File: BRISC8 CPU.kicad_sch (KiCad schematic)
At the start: 1 part, among them U101 27C256

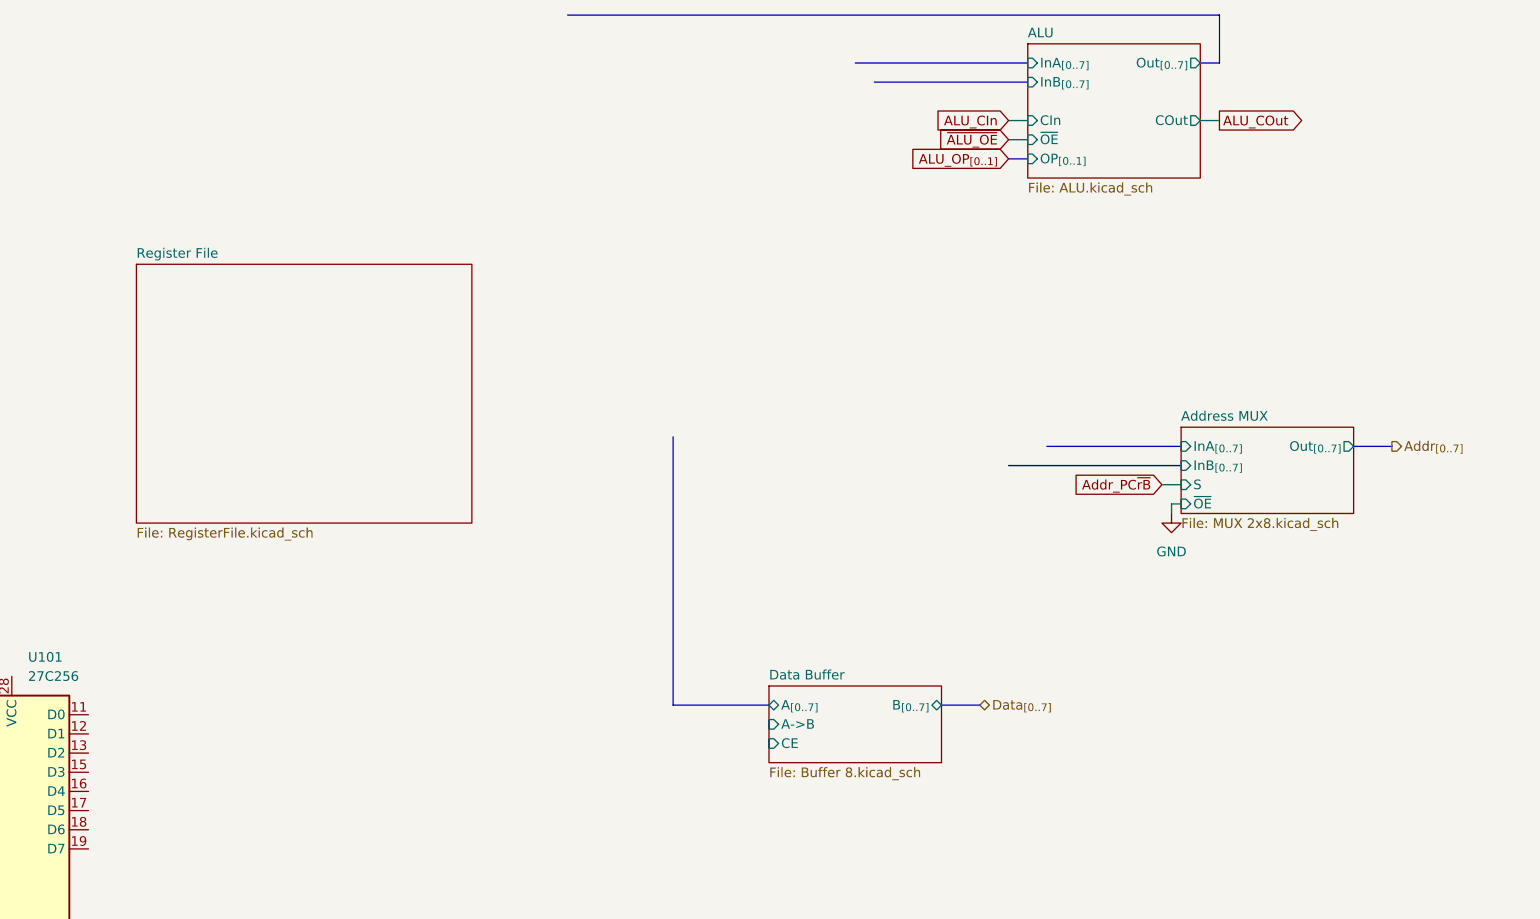
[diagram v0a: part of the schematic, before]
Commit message: Reorganize Registerfile
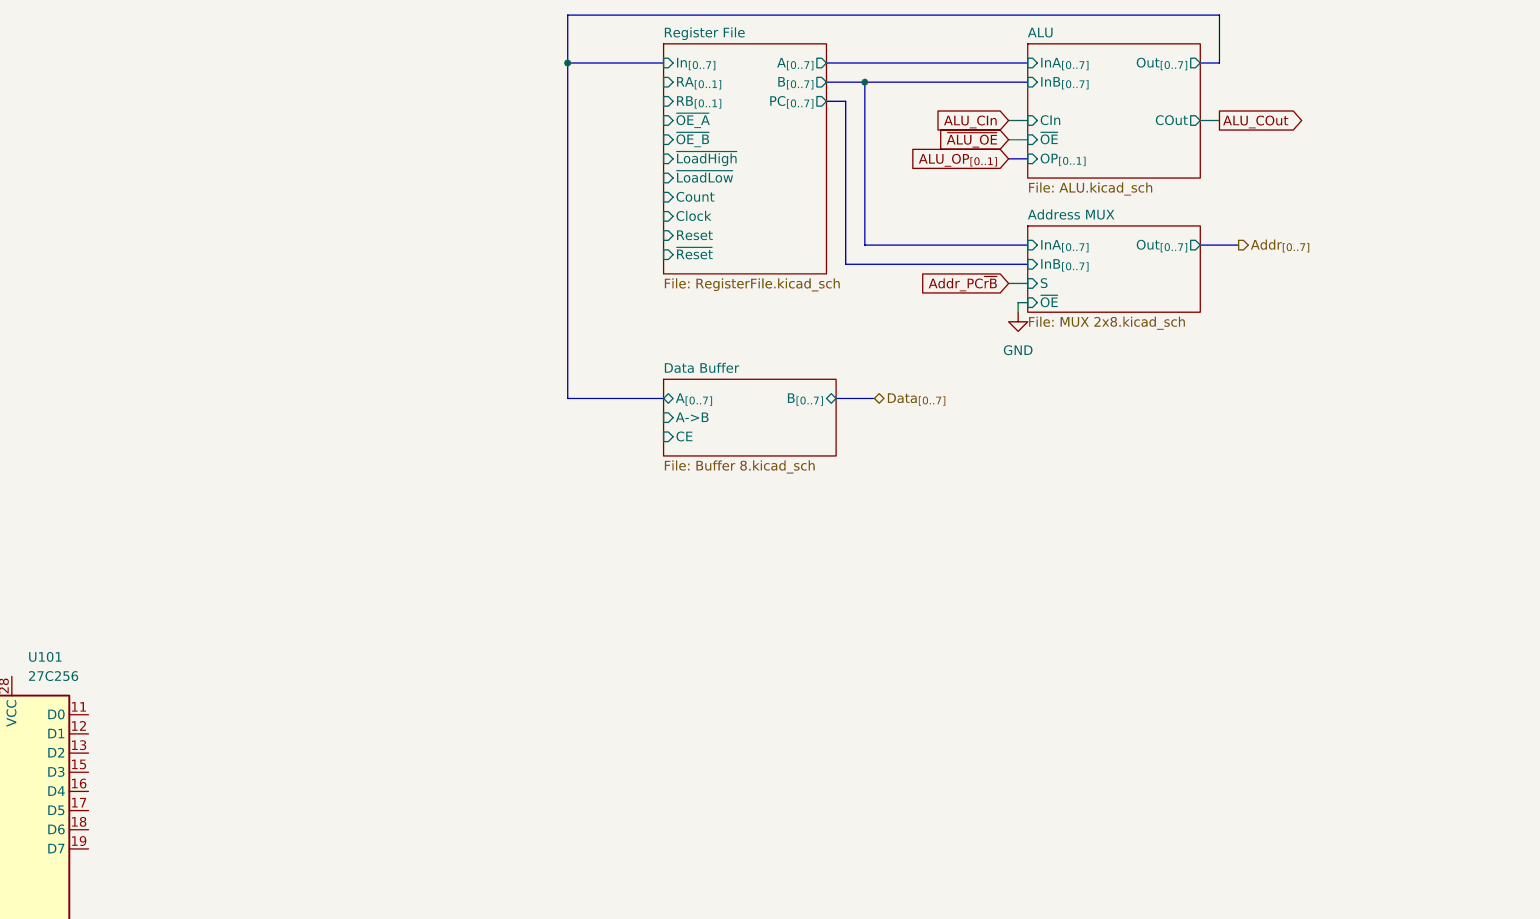
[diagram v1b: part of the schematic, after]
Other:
- sheet Register File ports: added A_{[0..7]}, B_{[0..7]}, Clock, Count, In_{[0..7]}, PC_{[0..7]}, RA_{[0..1]}, RB_{[0..1]}, Reset, ~{LoadHigh}, ~{LoadLow}, ~{OE_A}, ~{OE_B}, ~{Reset}; removed none

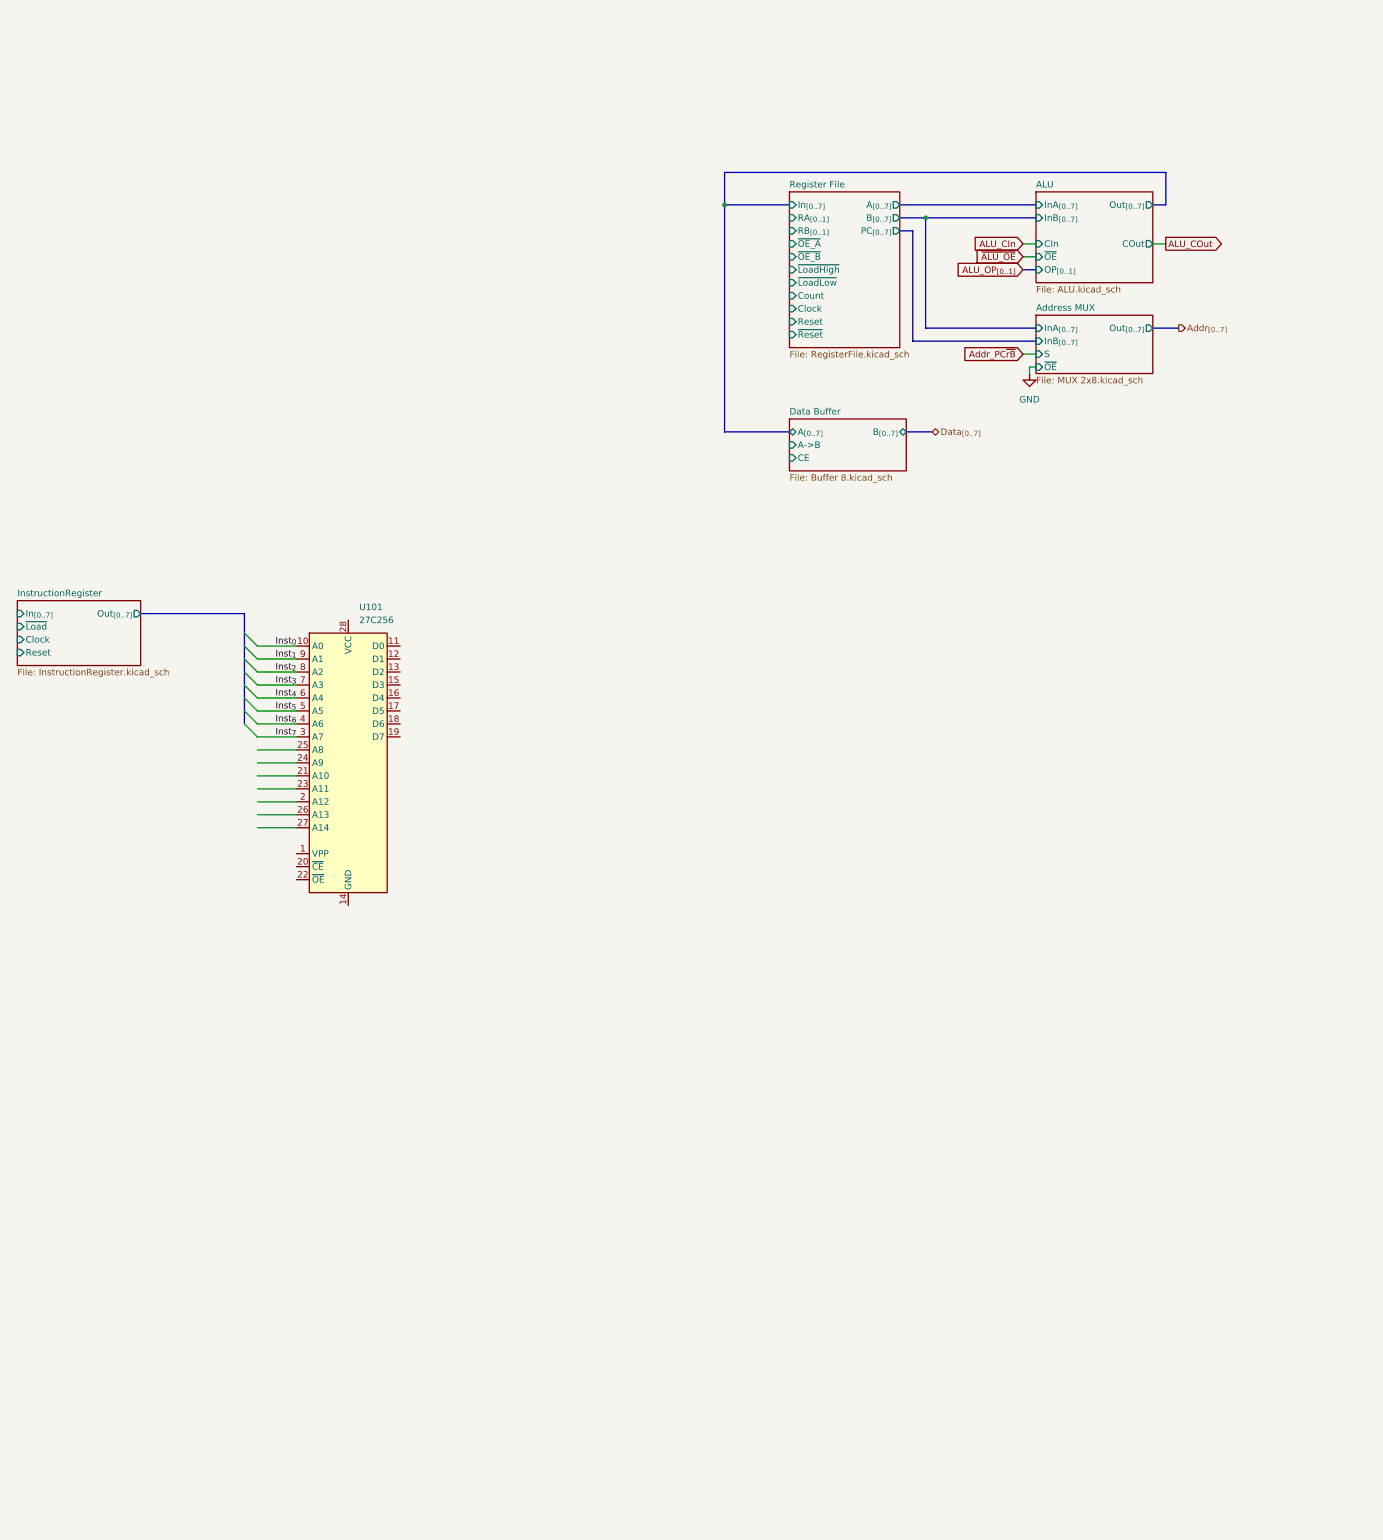
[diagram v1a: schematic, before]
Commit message: More cleanup and preparing signals for control logic
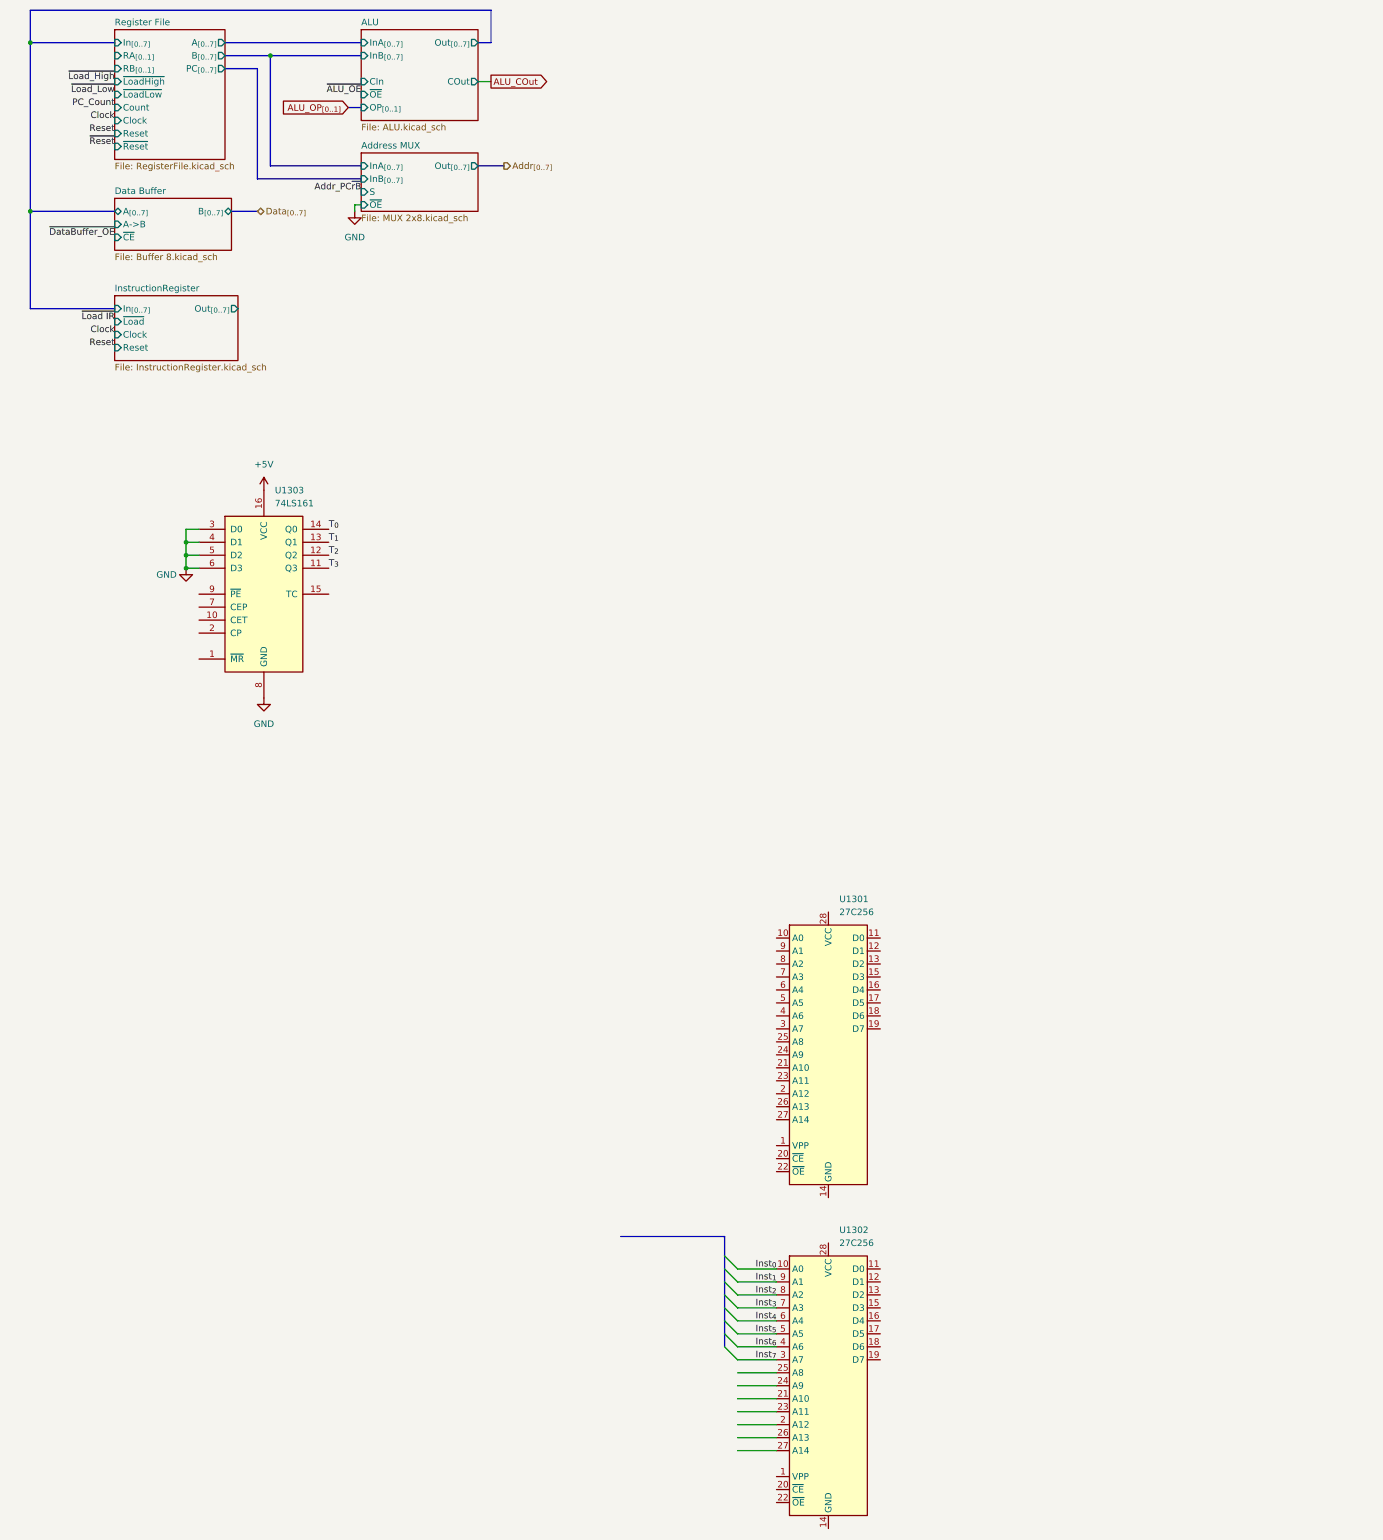
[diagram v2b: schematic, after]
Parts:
- added U1301: 27C256, Package_DIP:DIP-28_W15.24mm, symbol Memory_EPROM:27C256
- added U1303: 74LS161, symbol 74xx:74LS161
- renumbered U101 to U1302
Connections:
- net GND: now also U1303.3 (D0), U1303.4 (D1), U1303.5 (D2), U1303.6 (D3), U1303.8 (GND)
- new net +5V: U1303.16 (VCC)
- new net T_{0}: U1303.14 (Q0)
- new net T_{1}: U1303.13 (Q1)
- new net T_{2}: U1303.12 (Q2)
- new net T_{3}: U1303.11 (Q3)
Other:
- sheet Data Buffer ports: added ~{CE}; removed CE
- sheet Register File ports: added none; removed ~{OE_A}, ~{OE_B}
- moved on the sheet: U1302

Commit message: Fixed(?)
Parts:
- removed U1301, U1302: 27C256, Package_DIP:DIP-28_W15.24mm, symbol Memory_EPROM:27C256
- removed U1303: 74LS161, symbol 74xx:74LS161
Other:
- added sheet InstructionDecode (InstructionDecode.kicad_sch)

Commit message: Draft Schematic
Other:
- sheet ALU ports: added InA_Negative; removed CIn, COut
- sheet InstructionDecode ports: added ALU_OP_{[0..1]}, InA_Negative, ~{ALU OE}; removed none
- company: (none) -> Brian Duffy
- title: (none) -> BRISC8 CPU
